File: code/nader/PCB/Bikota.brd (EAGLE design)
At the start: 83.8 x 78.4 mm, 27 parts, among them Q1 IRLML6244

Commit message: Add files via upload
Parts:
- removed JP7: (no value), pinhead:1X01
- added C2, C3, C4, C5, C6, C7: 10uF, rcl:C0805
- moved R2 9.67 mm to (40.9, 53.3)
- moved R3 9.25 mm to (36.8, 53.3)
- moved Q1 8.98 mm to (33.0, 53.3)
- moved R1 8.52 mm to (21.6, 15.2)
- moved JP1 6.84 mm to (5.08, 67.3)
- moved JP6 2.00 mm to (38.1, 64.0)
- moved LED1 1.80 mm to (11.2, 62.1), turned to 180 degrees
- moved F1 1.80 mm to (19.1, 71.6), turned to 180 degrees
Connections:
- net ESP3V3: now also C4.1, C7.1
- net ESP5V: now also C2.1, C3.1, C5.1, C6.1
- net GND: now also C2.2, C4.2; no longer JP7.1
- net MOSFET_GND: now also C3.2, C5.2, C6.2, C7.2
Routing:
- net ESP5V: track 159.9 -> 180.1 mm, vias 2 -> 5
- net MOSFET_GND: track 129.5 -> 148.9 mm, vias 2 -> 1
- net ESP3V3: track 93.8 -> 111.1 mm, vias 0 -> 2
- net N$2: track 18.4 -> 9.21 mm
- net MOSFET: track 19.8 -> 10.9 mm
- net N$41: track 6.80 -> 13.4 mm
- net VBAT+: track 26.9 -> 22.6 mm
- net N$4: track 9.61 -> 7.14 mm
- net N$17: track 7.45 -> 9.45 mm
- net EP_DIN: track 50.6 -> 49.4 mm
- net ACC_INT: track 47.7 -> 47.0 mm
- net GND: track 62.6 -> 63.1 mm, vias 0 -> 104
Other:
- board text added: "+ -"
- board text added: "+ - 10 25"
- board text added: "+ - A"
- board text added: "+ R T -"
- board text added: "- +"
- board text added: "."
- board text added: "3-5V"
- board text added: "BME"
- board text added: "CO2"
- board text added: "F1"
- board text added: "GIT: XXXXXXX"
- board text added: "GPS"
- board text added: "Hochschule Rhein-Waal Applied Research Project B Supervisor: Prof. Dr. Timo Kahl Andreas Markwart (12186), Thi-Yen-Thu Nguyen (17913), Sarah-Maria Rostalski (17027), Francisco Susana (26574), Nader Kaake (14992) github.com/yenthusiastic/arp_b"
- board text added: "JLCJLCJLCJLC"
- board text added: "LED"
- board text added: "PM"
- board text added: "SCL SDA"
- board text added: "U1V11F5"
- board text added: "VIN GND VOUT"
- board text added: "ePaper"
- board text removed: "Hochschule Rhein-Waal Applied Research Project B Prof. Dr. Timo Kahl Andreas Markwart (12186), Thi-Yen-Thu Nguyen (17913), Sarah-Maria Rostalski (17027), Francisco Susana (26574), Nader Kaake (14992) GIT: XXXXXXX"

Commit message: Upload V0.1 of PCB
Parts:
- added C8: 10uF, rcl:C0805
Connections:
- net ESP5V: now also C8.1
- net GND: now also C8.2
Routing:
- net MOSFET_GND: track 148.9 -> 162.2 mm
- net ESP5V: track 180.1 -> 186.7 mm
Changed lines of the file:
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@@
 <attribute name="SPICEPREFIX" value="C" x="38.735" y="19.685" size="0.762" layer="27" display="off"/>
+</element>
+<element name="C8" library="rcl" library_urn="urn:adsk.eagle:library:334" package="C0805" package3d_urn="urn:adsk.eagle:package:23617/2" value="10uF" x="25.209" y="51.785" smashed="yes" rot="R90">
+<attribute name="NAME" x="23.939" y="50.515" size="1.27" layer="25" rot="R90"/>
+<attribute name="POPULARITY" value="63" x="25.209" y="51.785" size="1.778" layer="27" rot="R90" display="off"/>
+<attribute name="SPICEPREFIX" value="C" x="25.209" y="51.785" size="1.778" layer="27" rot="R90" display="off"/>
 </element>
 </elements>
 <signals>
 <signal name="GND">
-<contactref element="U$1" pad="GND"/>
 <contactref element="JP1" pad="2"/>
 <contactref element="Q1" pad="2"/>
@@
 <contactref element="R6" pad="1"/>
 <contactref element="C1" pad="2"/>
-<contactref element="JP2" pad="7"/>
 <contactref element="U$1" pad="GND3"/>
 <contactref element="JP3" pad="1"/>
@@
 <contactref element="U$8" pad="P$2"/>
 <contactref element="U$7" pad="P$2"/>
-<wire x1="40.64" y1="57.67501875" x2="40.64" y2="61.595" width="0.4064" layer="1"/>
 <wire x1="73.66" y1="27.432" x2="73.66" y2="31.22498125" width="0.4064" layer="1"/>
 <wire x1="58.42" y1="27.432" x2="58.42" y2="31.22498125" width="0.4064" layer="1"/>
@@
 <via x="24.095" y="7.001" extent="1-16" drill="0.3"/>
 <via x="25.655" y="1.938" extent="1-16" drill="0.3"/>
+<contactref element="U$1" pad="GND"/>
+<contactref element="JP2" pad="7"/>
+<wire x1="40.64" y1="57.67501875" x2="40.64" y2="61.595" width="0.4064" layer="1"/>
+<contactref element="C8" pad="2"/>
 </signal>
 <signal name="ACC_INT">
@@
 <wire x1="14.444" y1="66.421" x2="11.176" y2="63.153" width="0.4064" layer="1"/>
 <wire x1="27.94" y1="66.421" x2="14.444" y2="66.421" width="0.4064" layer="1"/>
-<wire x1="25.4" y1="22.86" x2="22.86" y2="22.86" width="1.016" layer="16"/>
-<wire x1="20.32" y1="25.4" x2="22.86" y2="22.86" width="1.016" layer="16"/>
-<wire x1="20.32" y1="33.02" x2="21.59" y2="34.29" width="1.016" layer="16"/>
-<wire x1="21.59" y1="34.29" x2="25.4" y2="34.29" width="1.016" layer="16"/>
-<wire x1="25.4" y1="34.29" x2="27.94" y2="36.83" width="1.016" layer="16"/>
-<wire x1="20.32" y1="25.4" x2="20.32" y2="33.02" width="1.016" layer="16"/>
 <via x="27.94" y="52.07" extent="1-16" drill="1"/>
 <wire x1="27.94" y1="52.07" x2="27.94" y2="57.67501875" width="1.016" layer="16"/>
 <via x="27.94" y="43.18" extent="1-16" drill="1"/>
-<wire x1="27.94" y1="43.18" x2="27.94" y2="52.07" width="1.016" layer="1"/>
-<wire x1="27.94" y1="36.83" x2="27.94" y2="43.18" width="1.016" layer="16"/>
+<wire x1="27.94" y1="43.18" x2="27.94" y2="51" width="1.016" layer="1"/>
+<wire x1="27.94" y1="51" x2="27.94" y2="52.07" width="1.016" layer="1"/>
 <wire x1="27.94" y1="66.421" x2="35.941" y2="66.421" width="1.016" layer="1"/>
 <contactref element="C2" pad="1"/>
@@
 <via x="66.675" y="74.422" extent="1-16" drill="1"/>
 <wire x1="66.675" y1="74.422" x2="68.773" y2="74.422" width="1.016" layer="1"/>
-<wire x1="22.225" y1="22.794" x2="22.291" y2="22.86" width="1.016" layer="1"/>
-<wire x1="22.291" y1="22.86" x2="25.4" y2="22.86" width="1.016" layer="1"/>
 <wire x1="35.941" y1="66.421" x2="37.719" y2="68.199" width="1.016" layer="1"/>
 <wire x1="37.719" y1="68.199" x2="38.608" y2="68.199" width="1.016" layer="1"/>
 <via x="38.608" y="68.199" extent="1-16" drill="1"/>
 <wire x1="38.608" y1="68.199" x2="41.529" y2="71.12" width="1.016" layer="16"/>
+<wire x1="25.4" y1="22.86" x2="22.291" y2="22.86" width="1.016" layer="1"/>
+<wire x1="22.291" y1="22.86" x2="22.225" y2="22.794" width="1.016" layer="1"/>
+<wire x1="25.4" y1="22.86" x2="21.14" y2="22.86" width="1.016" layer="16"/>
+<wire x1="21.14" y1="22.86" x2="19" y2="25" width="1.016" layer="16"/>
+<wire x1="19" y1="25" x2="19" y2="33.478" width="1.016" layer="16"/>
+<wire x1="27" y1="35" x2="28" y2="36" width="1.016" layer="16"/>
+<wire x1="28" y1="36" x2="28" y2="43.12" width="1.016" layer="16"/>
+<wire x1="28" y1="43.12" x2="27.94" y2="43.18" width="1.016" layer="16"/>
+<wire x1="19" y1="33.478" x2="20.522" y2="35" width="1.016" layer="16"/>
+<wire x1="20.522" y1="35" x2="27" y2="35" width="1.016" layer="16"/>
+<contactref element="C8" pad="1"/>
+<wire x1="25.209" y1="50.835" x2="27.775" y2="50.835" width="1.016" layer="1"/>
+<wire x1="27.775" y1="50.835" x2="27.94" y2="51" width="1.016" layer="1"/>
 </signal>
 <signal name="SDA">
@@
 <wire x1="32.85" y1="52.07" x2="33.02" y2="52.24" width="0.508" layer="1"/>
 <wire x1="22.54" y1="54.61" x2="27.94" y2="54.61" width="0.508" layer="1"/>
-<wire x1="29.2354" y1="25.4254" x2="27.94" y2="24.13" width="0.508" layer="16"/>
-<wire x1="29.2354" y1="25.4254" x2="29.2354" y2="33.50151875" width="0.508" layer="16"/>
-<wire x1="27.94" y1="24.13" x2="27.94" y2="22.86" width="0.508" layer="16"/>
-<wire x1="30.48" y1="34.74611875" x2="30.48" y2="43.18" width="0.508" layer="16"/>
-<via x="30.48" y="43.18" extent="1-16" drill="1"/>
-<wire x1="30.48" y1="43.18" x2="30.48" y2="49.7" width="0.508" layer="1"/>
-<wire x1="29.2354" y1="33.50151875" x2="30.48" y2="34.74611875" width="0.508" layer="16"/>
-<wire x1="30.48" y1="49.7" x2="33.02" y2="52.24" width="0.508" layer="1"/>
 <wire x1="33.02" y1="52.24" x2="34.841" y2="50.419" width="0.4064" layer="1"/>
 <wire x1="43.561" y1="50.419" x2="46.101" y2="47.879" width="0.4064" layer="1"/>
@@
 <wire x1="40.64" y1="22.86" x2="40.64" y2="20.64" width="1.016" layer="1"/>
 <wire x1="40.64" y1="20.64" x2="39.685" y2="19.685" width="1.016" layer="1"/>
+<wire x1="33.02" y1="52.24" x2="30" y2="49.22" width="1.016" layer="1"/>
+<via x="30" y="43" extent="1-16" drill="0.35"/>
+<wire x1="30" y1="49.22" x2="30" y2="43" width="1.016" layer="1"/>
+<wire x1="30" y1="43" x2="30" y2="35.635" width="1.016" layer="16"/>
+<wire x1="30" y1="35.635" x2="27.873" y2="33.508" width="1.016" layer="16"/>
+<wire x1="21.316" y1="33.508" x2="20.574" y2="32.766" width="1.016" layer="16"/>
+<wire x1="20.574" y1="32.766" x2="20.574" y2="25.918" width="1.016" layer="16"/>
+<wire x1="20.574" y1="25.918" x2="21.619" y2="24.873" width="1.016" layer="16"/>
+<wire x1="27.127" y1="24.873" x2="28" y2="24" width="1.016" layer="16"/>
+<wire x1="28" y1="24" x2="28" y2="22.92" width="1.016" layer="16"/>
+<wire x1="28" y1="22.92" x2="27.94" y2="22.86" width="1.016" layer="16"/>
+<wire x1="27.873" y1="33.508" x2="21.316" y2="33.508" width="1.016" layer="16"/>
+<wire x1="21.619" y1="24.873" x2="27.127" y2="24.873" width="1.016" layer="16"/>
 </signal>
 <signal name="N$6">

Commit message: Update V0.1
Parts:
- moved C8 4.44 mm to (28.8, 54.4), turned to 0 degrees
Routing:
- net GND: track 63.1 -> 41.9 mm, vias 104 -> 102
- net ESP5V: track 186.7 -> 183.8 mm, vias 5 -> 4
- net ESP3V3: track 111.1 -> 113.4 mm
- net MOSFET_GND: track 162.2 -> 160.0 mm
- net PM10: track 28.5 -> 29.1 mm
- net PM25: track 28.5 -> 29.1 mm
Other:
- board text added: "GIT: D246BD9"
- board text removed: "GIT: XXXXXXX"

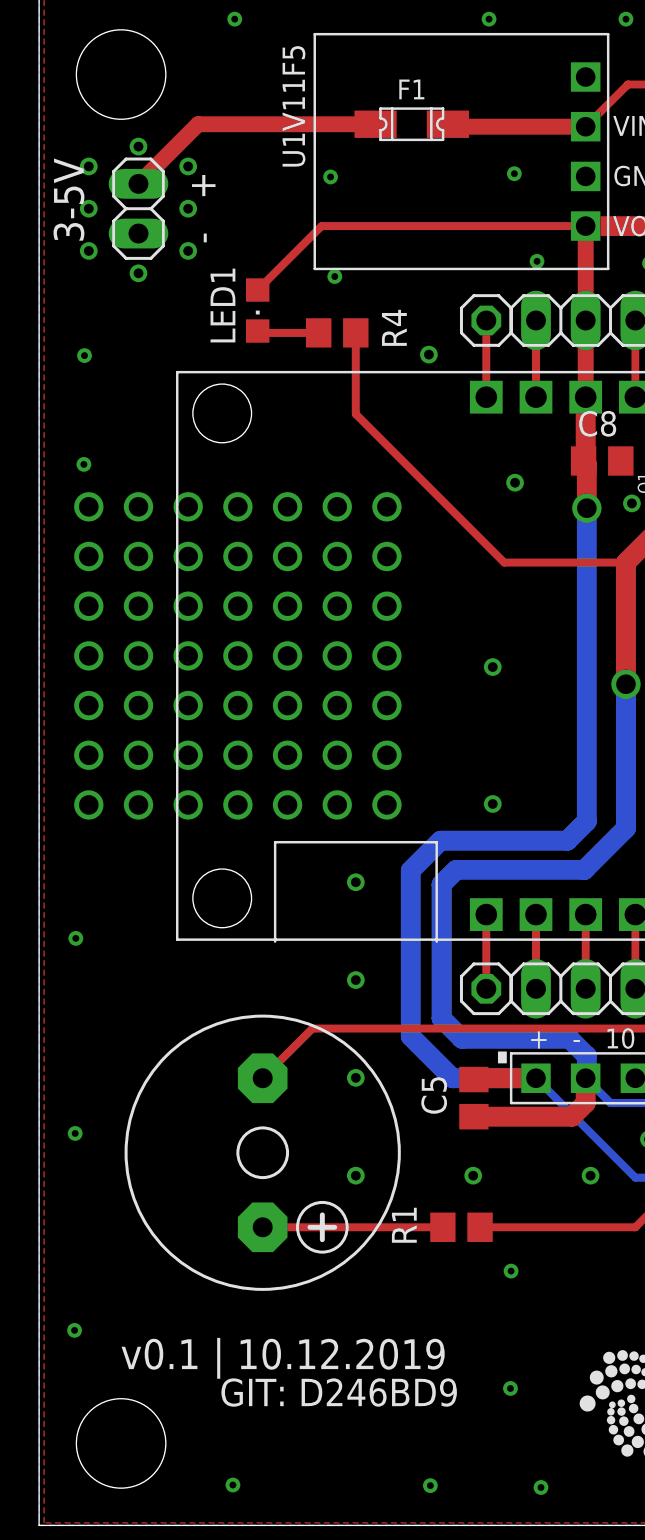
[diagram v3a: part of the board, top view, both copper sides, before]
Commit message: Update V0.1
- put "3-5V" below the input socket
- named the mosfet-led "MOSFET" instead of "LED1"
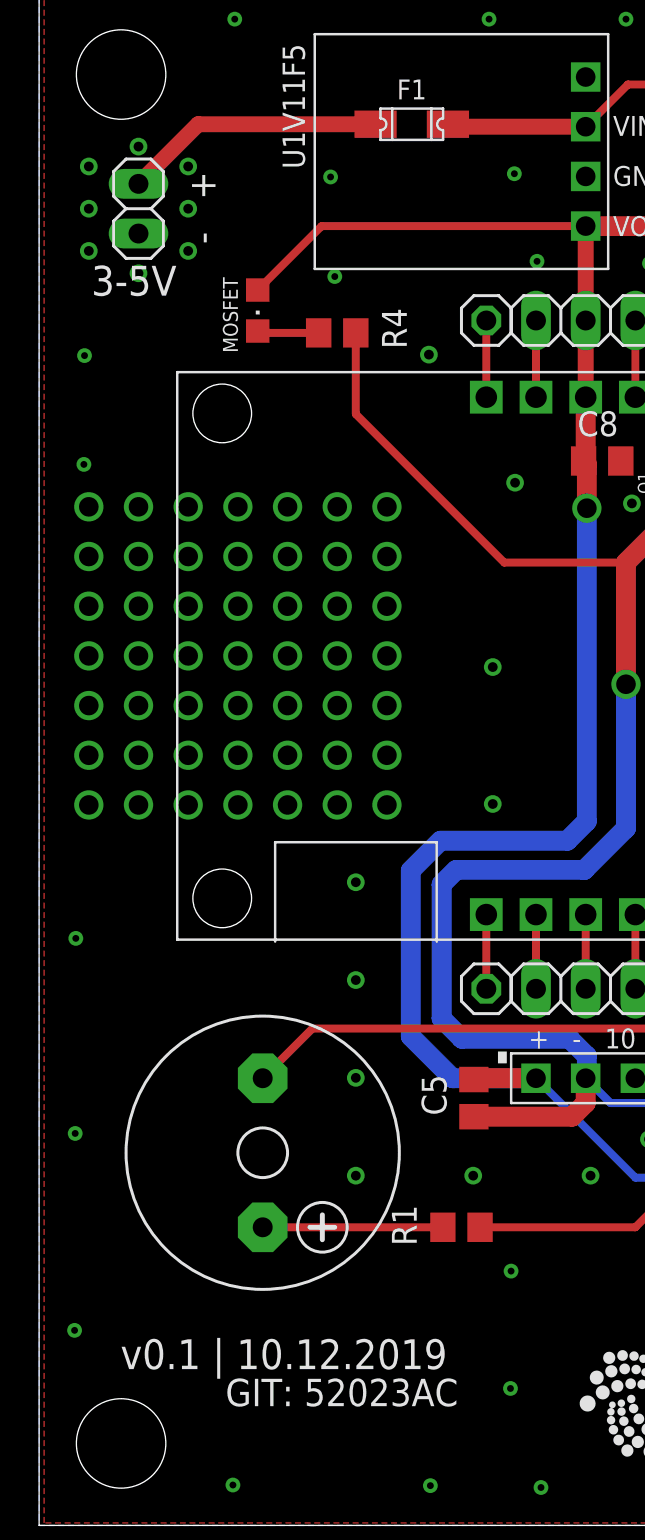
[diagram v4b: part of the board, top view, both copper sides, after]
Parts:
- renumbered LED1 to MOSFET
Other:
- board text added: "GIT: 52023AC"
- board text removed: "GIT: D246BD9"
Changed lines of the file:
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@@
 <dimension x1="0" y1="78.41" x2="0" y2="0" x3="-5" y3="39.205" textsize="1.778" layer="48" dtype="horizontal"/>
 <text x="18.288" y="72.898" size="1.016" layer="25">F1</text>
-<text x="9.223" y="6.096" size="1.397" layer="25" font="vector">GIT: D246BD9</text>
+<text x="9.525" y="6.096" size="1.397" layer="25" font="vector">GIT: 52023AC</text>
 <text x="22.987" y="23.622" size="3.556" layer="25">.</text>
 <text x="35.687" y="23.622" size="3.556" layer="25">.</text>
@@
 <text x="54.102" y="72.517" size="3.556" layer="25">.</text>
 <text x="64.262" y="72.517" size="3.556" layer="25">.</text>
-<text x="2.286" y="65.532" size="1.524" layer="25" font="vector" rot="R90">3-5V</text>
+<text x="2.667" y="62.865" size="1.524" layer="25" font="vector">3-5V</text>
 <text x="29.337" y="65.913" size="1.016" layer="25" font="vector" distance="26">VIN
 GND
@@
 <attribute name="SPICEPREFIX" value="R" x="15.24" y="60.96" size="1.778" layer="27" rot="R180" display="off"/>
 </element>
-<element name="LED1" library="led" library_urn="urn:adsk.eagle:library:259" package="CHIPLED_0805" package3d_urn="urn:adsk.eagle:package:15821/2" value="" x="11.176" y="62.103" smashed="yes" rot="R180">
-<attribute name="NAME" x="8.763" y="64.389" size="1.27" layer="25" rot="R270"/>
+<element name="MOSFET" library="led" library_urn="urn:adsk.eagle:library:259" package="CHIPLED_0805" package3d_urn="urn:adsk.eagle:package:15821/2" value="" x="11.176" y="62.103" smashed="yes" rot="R180">
+<attribute name="NAME" x="10.16" y="59.944" size="0.762" layer="25" rot="R90"/>
 <attribute name="POPULARITY" value="52" x="11.176" y="62.103" size="1.778" layer="27" rot="R180" display="off"/>
 <attribute name="VALUE" x="8.636" y="63.373" size="1.27" layer="27" rot="R270"/>
@@
 <signal name="ESP5V">
 <contactref element="U$1" pad="ESP32_5V"/>
-<contactref element="LED1" pad="A"/>
+<contactref element="MOSFET" pad="A"/>
 <contactref element="U$5" pad="P$1"/>
 <contactref element="U$6" pad="P$1"/>
@@
 <signal name="N$6">
 <contactref element="R4" pad="2"/>
-<contactref element="LED1" pad="C"/>
+<contactref element="MOSFET" pad="C"/>
 <wire x1="11.176" y1="61.053" x2="11.269" y2="60.96" width="0.4064" layer="1"/>
 <wire x1="11.269" y1="60.96" x2="14.29" y2="60.96" width="0.4064" layer="1"/>

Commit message: Upload V0.1 final
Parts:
- moved C8 2.09 mm to (26.9, 55.4), turned to 180 degrees
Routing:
- net ESP5V: track 183.8 -> 186.1 mm, vias 4 -> 5
- net MOSFET_GND: track 160.0 -> 161.7 mm
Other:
- board text added: "GIT: 9CA7C4E"
- board text removed: "GIT: 52023AC"
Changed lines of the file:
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@@
 <layer number="14" name="Route14" color="22" fill="1" visible="no" active="no"/>
 <layer number="15" name="Route15" color="23" fill="1" visible="no" active="no"/>
-<layer number="16" name="Bottom" color="1" fill="1" visible="yes" active="yes"/>
+<layer number="16" name="Bottom" color="1" fill="1" visible="no" active="yes"/>
 <layer number="17" name="Pads" color="2" fill="1" visible="yes" active="yes"/>
 <layer number="18" name="Vias" color="2" fill="1" visible="yes" active="yes"/>
@@
 <dimension x1="0" y1="78.41" x2="0" y2="0" x3="-5" y3="39.205" textsize="1.778" layer="48" dtype="horizontal"/>
 <text x="18.288" y="72.898" size="1.016" layer="25">F1</text>
-<text x="9.525" y="6.096" size="1.397" layer="25" font="vector">GIT: 52023AC</text>
+<text x="9.906" y="6.096" size="1.397" layer="25" font="vector">GIT: 9CA7C4E</text>
 <text x="22.987" y="23.622" size="3.556" layer="25">.</text>
 <text x="35.687" y="23.622" size="3.556" layer="25">.</text>
@@
 <text x="64.262" y="72.517" size="3.556" layer="25">.</text>
 <text x="2.667" y="62.865" size="1.524" layer="25" font="vector">3-5V</text>
-<text x="29.337" y="65.913" size="1.016" layer="25" font="vector" distance="26">VIN
+<text x="29.464" y="65.786" size="1.016" layer="25" font="vector" distance="26">VIN
 GND
 VOUT</text>
@@
 <attribute name="SPICEPREFIX" value="C" x="38.735" y="19.685" size="0.762" layer="27" display="off"/>
 </element>
-<element name="C8" library="rcl" library_urn="urn:adsk.eagle:library:334" package="C0805" package3d_urn="urn:adsk.eagle:package:23617/2" value="10uF" x="28.785" y="54.41" smashed="yes">
-<attribute name="NAME" x="27.515" y="55.68" size="1.27" layer="25"/>
-<attribute name="POPULARITY" value="63" x="28.785" y="54.41" size="1.778" layer="27" display="off"/>
-<attribute name="SPICEPREFIX" value="C" x="28.785" y="54.41" size="1.778" layer="27" display="off"/>
+<element name="C8" library="rcl" library_urn="urn:adsk.eagle:library:334" package="C0805" package3d_urn="urn:adsk.eagle:package:23617/2" value="10uF" x="26.914" y="55.352" smashed="yes" rot="R180">
+<attribute name="NAME" x="28.184" y="54.082" size="1.27" layer="25" rot="R180"/>
+<attribute name="POPULARITY" value="63" x="26.914" y="55.352" size="1.778" layer="27" rot="R180" display="off"/>
+<attribute name="SPICEPREFIX" value="C" x="26.914" y="55.352" size="1.778" layer="27" rot="R180" display="off"/>
 </element>
 </elements>
@@
 <via x="45.1" y="51.733" extent="1-16" drill="0.5"/>
 <via x="38.835" y="55.74" extent="1-16" drill="0.5"/>
-<via x="24.33" y="53.302" extent="1-16" drill="0.5"/>
+<via x="23.33" y="54.302" extent="1-16" drill="0.5"/>
 <via x="23.19" y="43.879" extent="1-16" drill="0.5"/>
 <via x="23.19" y="36.879" extent="1-16" drill="0.5"/>
@@
 <wire x1="40.64" y1="57.67501875" x2="40.64" y2="61.595" width="0.4064" layer="1"/>
 <contactref element="C8" pad="2"/>
-<via x="30.302" y="52.245" extent="1-16" drill="0.5"/>
+<via x="30.048" y="54.277" extent="1-16" drill="0.5"/>
 </signal>
 <signal name="ACC_INT">
@@
 <wire x1="21.14" y1="22.86" x2="19" y2="25" width="1.016" layer="16"/>
 <wire x1="19" y1="25" x2="19" y2="33.478" width="1.016" layer="16"/>
-<wire x1="28" y1="36" x2="27" y2="35" width="1.016" layer="16"/>
+<wire x1="27" y1="35" x2="28" y2="36" width="1.016" layer="16"/>
 <wire x1="19" y1="33.478" x2="20.522" y2="35" width="1.016" layer="16"/>
 <wire x1="20.522" y1="35" x2="27" y2="35" width="1.016" layer="16"/>
 <contactref element="C8" pad="1"/>
-<wire x1="27.94" y1="57.67501875" x2="27.94" y2="54.515" width="1.016" layer="1"/>
-<wire x1="27.94" y1="54.515" x2="27.835" y2="54.41" width="1.016" layer="1"/>
-<wire x1="27.835" y1="54.41" x2="28" y2="54.245" width="1.016" layer="1"/>
-<wire x1="28" y1="54.245" x2="28" y2="52" width="1.016" layer="1"/>
-<via x="28" y="52" extent="1-16" drill="1"/>
-<wire x1="28" y1="52" x2="28" y2="36" width="1.016" layer="16"/>
+<wire x1="28" y1="36" x2="28" y2="43" width="1.016" layer="16"/>
+<via x="28" y="43" extent="1-16" drill="1"/>
+<wire x1="28" y1="43" x2="28" y2="49.343" width="1.016" layer="1"/>
+<wire x1="28" y1="49.343" x2="27.94" y2="49.403" width="1.016" layer="1"/>
+<via x="27.94" y="49.403" extent="1-16" drill="1"/>
+<wire x1="27.94" y1="49.403" x2="27.94" y2="57.67501875" width="1.016" layer="16"/>
+<wire x1="27.864" y1="57.59901875" x2="27.94" y2="57.67501875" width="1.016" layer="1"/>
+<wire x1="27.864" y1="55.352" x2="27.864" y2="57.59901875" width="1.016" layer="1"/>
 </signal>
 <signal name="SDA">
@@
 <wire x1="33.147" y1="49.403" x2="33.147" y2="54.9013125" width="0.508" layer="16"/>
 <via x="33.147" y="49.403" extent="1-16" drill="1"/>
-<wire x1="33.147" y1="49.403" x2="33.147" y2="43.307" width="0.508" layer="1"/>
-<wire x1="33.147" y1="43.307" x2="33.02" y2="43.18" width="0.508" layer="1"/>
-<via x="33.02" y="43.18" extent="1-16" drill="1"/>
-<wire x1="33.02" y1="43.18" x2="33.02" y2="36.83" width="0.508" layer="16"/>
 <wire x1="36.8554" y1="32.9946" x2="36.8554" y2="24.1046" width="0.508" layer="16"/>
-<wire x1="33.02" y1="36.83" x2="36.8554" y2="32.9946" width="0.508" layer="16"/>
+<wire x1="36.8554" y1="32.9946" x2="33.02" y2="36.83" width="0.508" layer="16"/>
 <wire x1="36.8554" y1="24.1046" x2="38.1" y2="22.86" width="0.508" layer="16"/>
 <contactref element="C4" pad="1"/>
@@
 <wire x1="36.8554" y1="56.6674" x2="36.9062" y2="56.7182" width="0.4064" layer="16"/>
 <wire x1="36.9062" y1="56.7182" x2="36.9062" y2="58.6605125" width="0.4064" layer="16"/>
+<wire x1="33.02" y1="36.83" x2="33" y2="36.85" width="0.4064" layer="16"/>
+<wire x1="33" y1="36.85" x2="33" y2="43" width="0.4064" layer="16"/>
+<via x="33" y="43" extent="1-16" drill="1"/>
+<wire x1="33" y1="43" x2="33" y2="49.256" width="0.4064" layer="1"/>
+<wire x1="33" y1="49.256" x2="33.147" y2="49.403" width="0.4064" layer="1"/>
 </signal>
 <signal name="MOSFET">
@@
 <wire x1="27.873" y1="33.508" x2="21.316" y2="33.508" width="1.016" layer="16"/>
 <wire x1="21.619" y1="24.873" x2="27.127" y2="24.873" width="1.016" layer="16"/>
-<wire x1="16.19" y1="60.96" x2="16.19" y2="56.81" width="0.4064" layer="1"/>
-<wire x1="23.78" y1="49.22" x2="30" y2="49.22" width="0.4064" layer="1"/>
-<wire x1="16.19" y1="56.81" x2="23.78" y2="49.22" width="0.4064" layer="1"/>
+<wire x1="16.19" y1="60.96" x2="16.19" y2="57" width="0.4064" layer="1"/>
 <wire x1="30" y1="49.22" x2="33.02" y2="52.24" width="1.016" layer="1"/>
+<wire x1="16.19" y1="57" x2="20.95" y2="52.24" width="0.4064" layer="1"/>
+<wire x1="20.95" y1="52.24" x2="33.02" y2="52.24" width="0.4064" layer="1"/>
 </signal>
 <signal name="N$6">
